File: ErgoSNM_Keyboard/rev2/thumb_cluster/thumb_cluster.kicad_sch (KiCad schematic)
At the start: 19 parts, among them J1 Conn_01x08

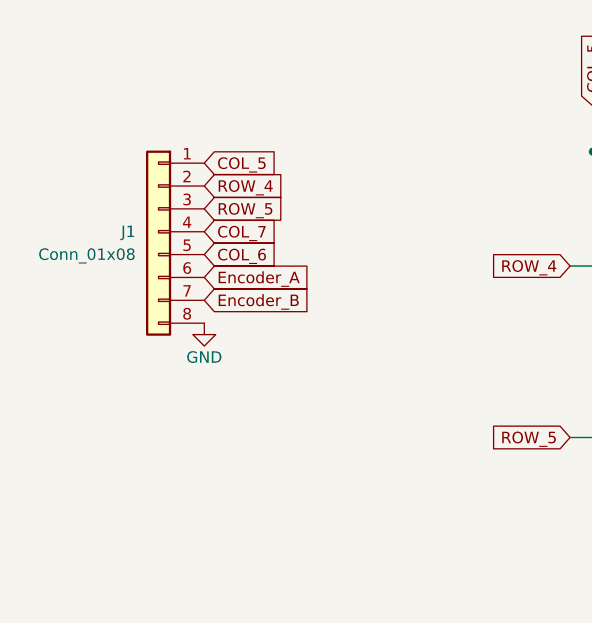
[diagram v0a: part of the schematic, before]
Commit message: Replace JST GH 1.25 connector with 0.5mm FPC
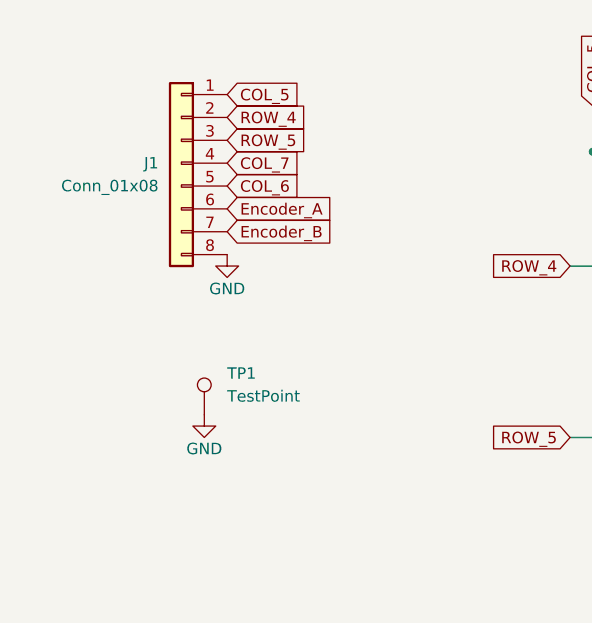
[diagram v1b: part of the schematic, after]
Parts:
- added TP1: TestPoint, TestPoint:TestPoint_Pad_D2.5mm, symbol Connector:TestPoint
- J1: footprint Connector_JST:JST_GH_SM08B-GHS-TB_1x08-1MP_P1.25mm_Horizontal -> ErgoSNM_Keyboard:FPC_8P_0.5mm_AFC01-S08FCA-00
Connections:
- net GND: now also TP1.1
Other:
- moved on the sheet: J1
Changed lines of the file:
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@@
     (stroke (width 0) (type default) (color 0 0 0 0))
   )
-  (global_label "COL_5" (shape input) (at 82.55 95.25 0) (fields_autoplaced)
-    (effects (font (size 1.27 1.27)) (justify left))
-    (property "Intersheet References" "${INTERSHEET_REFS}" (id 0) (at 90.7688 95.3294 0)
-      (effects (font (size 1.27 1.27)) (justify left) hide)
-    )
-  )
-  (global_label "Encoder_B" (shape input) (at 82.55 110.49 0) (fields_autoplaced)
-    (effects (font (size 1.27 1.27)) (justify left))
-    (property "Intersheet References" "${INTERSHEET_REFS}" (id 0) (at 94.7602 110.4106 0)
+  (global_label "COL_5" (shape input) (at 85.09 87.63 0) (fields_autoplaced)
+    (effects (font (size 1.27 1.27)) (justify left))
+    (property "Intersheet References" "${INTERSHEET_REFS}" (id 0) (at 93.3088 87.7094 0)
+      (effects (font (size 1.27 1.27)) (justify left) hide)
+    )
+  )
+  (global_label "Encoder_B" (shape input) (at 85.09 102.87 0) (fields_autoplaced)
+    (effects (font (size 1.27 1.27)) (justify left))
+    (property "Intersheet References" "${INTERSHEET_REFS}" (id 0) (at 97.3002 102.7906 0)
       (effects (font (size 1.27 1.27)) (justify left) hide)
     )
@@
     )
   )
-  (global_label "ROW_4" (shape input) (at 82.55 97.79 0) (fields_autoplaced)
-    (effects (font (size 1.27 1.27)) (justify left))
-    (property "Intersheet References" "${INTERSHEET_REFS}" (id 0) (at 91.1921 97.7106 0)
+  (global_label "ROW_4" (shape input) (at 85.09 90.17 0) (fields_autoplaced)
+    (effects (font (size 1.27 1.27)) (justify left))
+    (property "Intersheet References" "${INTERSHEET_REFS}" (id 0) (at 93.7321 90.0906 0)
       (effects (font (size 1.27 1.27)) (justify left) hide)
     )
@@
     )
   )
-  (global_label "COL_6" (shape input) (at 82.55 105.41 0) (fields_autoplaced)
-    (effects (font (size 1.27 1.27)) (justify left))
-    (property "Intersheet References" "${INTERSHEET_REFS}" (id 0) (at 90.7688 105.3306 0)
+  (global_label "COL_6" (shape input) (at 85.09 97.79 0) (fields_autoplaced)
+    (effects (font (size 1.27 1.27)) (justify left))
+    (property "Intersheet References" "${INTERSHEET_REFS}" (id 0) (at 93.3088 97.7106 0)
       (effects (font (size 1.27 1.27)) (justify left) hide)
     )
@@
     )
   )
-  (global_label "Encoder_A" (shape input) (at 82.55 107.95 0) (fields_autoplaced)
-    (effects (font (size 1.27 1.27)) (justify left))
-    (property "Intersheet References" "${INTERSHEET_REFS}" (id 0) (at 94.5788 107.8706 0)
+  (global_label "Encoder_A" (shape input) (at 85.09 100.33 0) (fields_autoplaced)
+    (effects (font (size 1.27 1.27)) (justify left))
+    (property "Intersheet References" "${INTERSHEET_REFS}" (id 0) (at 97.1188 100.2506 0)
       (effects (font (size 1.27 1.27)) (justify left) hide)
     )
@@
     )
   )
-  (global_label "COL_7" (shape input) (at 82.55 102.87 0) (fields_autoplaced)
-    (effects (font (size 1.27 1.27)) (justify left))
-    (property "Intersheet References" "${INTERSHEET_REFS}" (id 0) (at 90.7688 102.7906 0)
+  (global_label "COL_7" (shape input) (at 85.09 95.25 0) (fields_autoplaced)
+    (effects (font (size 1.27 1.27)) (justify left))
+    (property "Intersheet References" "${INTERSHEET_REFS}" (id 0) (at 93.3088 95.1706 0)
       (effects (font (size 1.27 1.27)) (justify left) hide)
     )
@@
     )
   )
-  (global_label "ROW_5" (shape input) (at 82.55 100.33 0) (fields_autoplaced)
-    (effects (font (size 1.27 1.27)) (justify left))
-    (property "Intersheet References" "${INTERSHEET_REFS}" (id 0) (at 91.1921 100.2506 0)
+  (global_label "ROW_5" (shape input) (at 85.09 92.71 0) (fields_autoplaced)
+    (effects (font (size 1.27 1.27)) (justify left))
+    (property "Intersheet References" "${INTERSHEET_REFS}" (id 0) (at 93.7321 92.6306 0)
       (effects (font (size 1.27 1.27)) (justify left) hide)
     )
@@
     (pin "2")
   )
-  (symbol (lib_id "Connector_Generic:Conn_01x08") (at 77.47 102.87 0) (mirror y) (unit 1)
+  (symbol (lib_id "Connector_Generic:Conn_01x08") (at 80.01 95.25 0) (mirror y) (unit 1)
     (in_bom yes) (on_board yes) (fields_autoplaced)
-    (property "Reference" "J1" (id 0) (at 74.93 102.8699 0)
+    (property "Reference" "J1" (id 0) (at 77.47 95.2499 0)
       (effects (font (size 1.27 1.27)) (justify left))
     )
-    (property "Value" "Conn_01x08" (id 1) (at 74.93 105.4099 0)
+    (property "Value" "Conn_01x08" (id 1) (at 77.47 97.7899 0)
       (effects (font (size 1.27 1.27)) (justify left))
     )
-    (property "Footprint" "Connector_JST:JST_GH_SM08B-GHS-TB_1x08-1MP_P1.25mm_Horizontal" (id 2) (at 77.47 102.87 0)
-      (effects (font (size 1.27 1.27)) hide)
-    )
-    (property "Datasheet" "~" (id 3) (at 77.47 102.87 0)
-      (effects (font (size 1.27 1.27)) hide)
-    )
-    (property "LCSC" "C265111" (id 4) (at 77.47 102.87 0)
-      (effects (font (size 1.27 1.27)) hide)
-    )
-    (property "MFR. Part #" "SM08B-GHS-TB(LF)(SN)" (id 5) (at 77.47 102.87 0)
+    (property "Footprint" "ErgoSNM_Keyboard:FPC_8P_0.5mm_AFC01-S08FCA-00" (id 2) (at 80.01 95.25 0)
+      (effects (font (size 1.27 1.27)) hide)
+    )
+    (property "Datasheet" "~" (id 3) (at 80.01 95.25 0)
+      (effects (font (size 1.27 1.27)) hide)
+    )
+    (property "LCSC" "C265111" (id 4) (at 80.01 95.25 0)
+      (effects (font (size 1.27 1.27)) hide)
+    )
+    (property "MFR. Part #" "SM08B-GHS-TB(LF)(SN)" (id 5) (at 80.01 95.25 0)
       (effects (font (size 1.27 1.27)) hide)
     )
@@
     (pin "2")
   )
-  (symbol (lib_id "power:GND") (at 82.55 113.03 0) (mirror y) (unit 1)
-    (in_bom yes) (on_board yes)
-    (property "Reference" "#PWR0102" (id 0) (at 82.55 119.38 0)
-      (effects (font (size 1.27 1.27)) hide)
-    )
-    (property "Value" "GND" (id 1) (at 82.55 116.84 0))
-    (property "Footprint" "" (id 2) (at 82.55 113.03 0)
-      (effects (font (size 1.27 1.27)) hide)
-    )
-    (property "Datasheet" "" (id 3) (at 82.55 113.03 0)
+  (symbol (lib_id "power:GND") (at 85.09 105.41 0) (mirror y) (unit 1)
+    (in_bom yes) (on_board yes)
+    (property "Reference" "#PWR0102" (id 0) (at 85.09 111.76 0)
+      (effects (font (size 1.27 1.27)) hide)
+    )
+    (property "Value" "GND" (id 1) (at 85.09 109.22 0))
+    (property "Footprint" "" (id 2) (at 85.09 105.41 0)
+      (effects (font (size 1.27 1.27)) hide)
+    )
+    (property "Datasheet" "" (id 3) (at 85.09 105.41 0)
+      (effects (font (size 1.27 1.27)) hide)
+    )
+    (pin "1")
+  )
+  (symbol (lib_id "Connector:TestPoint") (at 82.55 123.19 0) (unit 1)
+    (in_bom yes) (on_board yes) (fields_autoplaced)
+    (property "Reference" "TP1" (id 0) (at 85.09 118.6179 0)
+      (effects (font (size 1.27 1.27)) (justify left))
+    )
+    (property "Value" "TestPoint" (id 1) (at 85.09 121.1579 0)
+      (effects (font (size 1.27 1.27)) (justify left))
+    )
+    (property "Footprint" "TestPoint:TestPoint_Pad_D2.5mm" (id 2) (at 87.63 123.19 0)
+      (effects (font (size 1.27 1.27)) hide)
+    )
+    (property "Datasheet" "~" (id 3) (at 87.63 123.19 0)
+      (effects (font (size 1.27 1.27)) hide)
+    )
+    (pin "1")
+  )
+  (symbol (lib_id "power:GND") (at 82.55 123.19 0) (mirror y) (unit 1)
+    (in_bom yes) (on_board yes)
+    (property "Reference" "#PWR0103" (id 0) (at 82.55 129.54 0)
+      (effects (font (size 1.27 1.27)) hide)
+    )
+    (property "Value" "GND" (id 1) (at 82.55 127 0))
+    (property "Footprint" "" (id 2) (at 82.55 123.19 0)
+      (effects (font (size 1.27 1.27)) hide)
+    )
+    (property "Datasheet" "" (id 3) (at 82.55 123.19 0)
       (effects (font (size 1.27 1.27)) hide)
     )
@@
       (reference "#PWR0102") (unit 1) (value "GND") (footprint "")
     )
+    (path "/7e767a08-4930-4303-b533-55705f310e64"
+      (reference "#PWR0103") (unit 1) (value "GND") (footprint "")
+    )
     (path "/14436e2f-3fca-4d37-ab24-59b0ddef80f7"
       (reference "D1") (unit 1) (value "1N4148") (footprint "Diode_SMD:D_SOD-123")
@@
     )
     (path "/4730308c-7fa3-4a93-87ee-eded711f7f1d"
-      (reference "J1") (unit 1) (value "Conn_01x08") (footprint "Connector_JST:JST_GH_SM08B-GHS-TB_1x08-1MP_P1.25mm_Horizontal")
+      (reference "J1") (unit 1) (value "Conn_01x08") (footprint "ErgoSNM_Keyboard:FPC_8P_0.5mm_AFC01-S08FCA-00")
     )
     (path "/8d338a05-136a-4618-999f-3da553cf9a12"
@@
       (reference "KEY6") (unit 1) (value "SW_Push_45deg") (footprint "key-switches:MX_switch_PTH_hotswap_A")
     )
-  )
+    (path "/77606055-ea6e-49a3-b70d-e0850b43e23a"
+      (reference "TP1") (unit 1) (value "TestPoint") (footprint "TestPoint:TestPoint_Pad_D2.5mm")
+    )
+  )

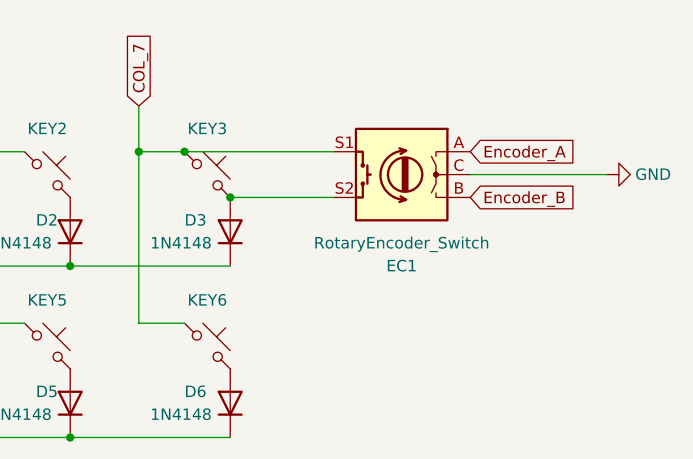
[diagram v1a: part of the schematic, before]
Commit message: Change license to CERN-OHL-P v2
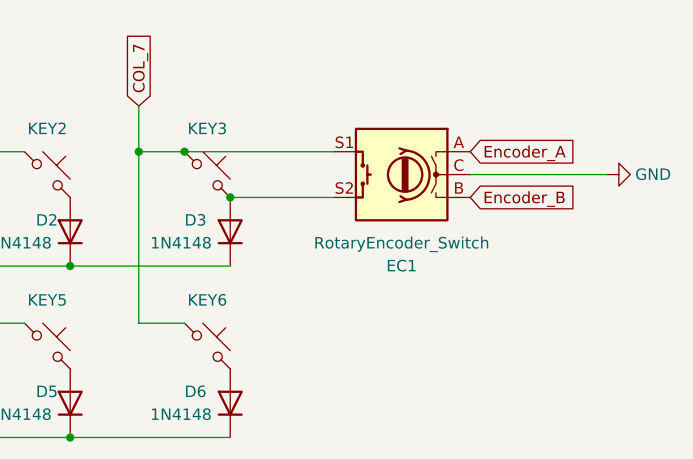
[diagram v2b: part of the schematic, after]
